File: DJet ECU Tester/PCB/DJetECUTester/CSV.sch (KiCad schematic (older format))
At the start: 1 part, among them U6 SFH617A-1X007T

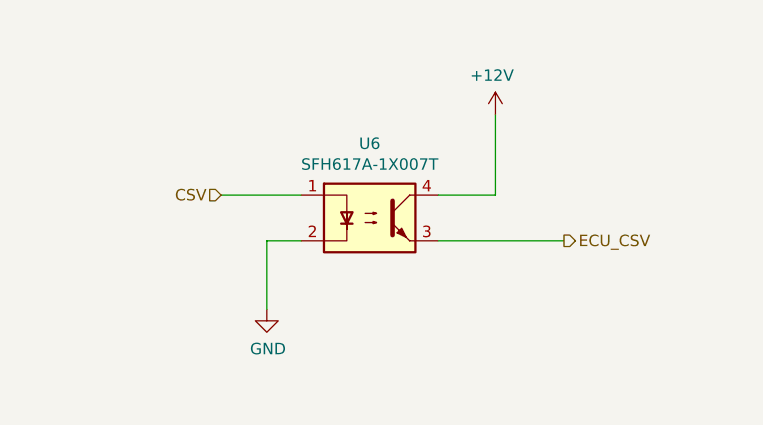
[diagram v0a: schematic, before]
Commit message: Working on PCB layout. Changed CSV circuit from optocoupler to transistors. Added decoupling caps for digital pots.
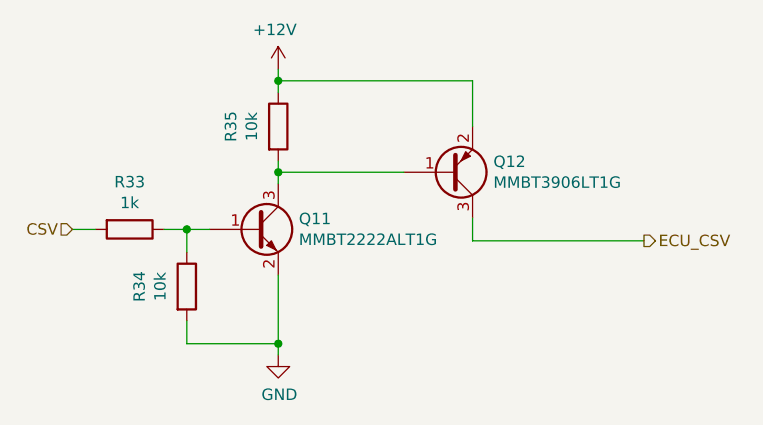
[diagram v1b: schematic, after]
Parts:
- removed U6: SFH617A-1X007T, Britishideas:SMD-4-OPTION7, symbol Isolator:SFH617A-1
- added Q11: MMBT2222ALT1G, Package_TO_SOT_SMD:SOT-23, symbol Transistor_BJT:MMBT3904
- added Q12: MMBT3906LT1G, Package_TO_SOT_SMD:SOT-23, symbol Device:Q_PNP_BEC
- added R33: 1k, Resistor_SMD:R_0805_2012Metric, symbol Device:R
- added R34, R35: 10k, Resistor_SMD:R_0805_2012Metric, symbol Device:R
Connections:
- net +12V: now also Q12.2 (E), R35.1
- net CSV: now also R33.2
- net ECU_CSV: now also Q12.3 (C)
- net GND: now also Q11.2 (E), R34.2
- new net: Q11.1 (B), R33.1, R34.1
- new net: Q11.3 (C), Q12.1 (B), R35.2
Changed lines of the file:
@@
 Sheet 7 7
 Title "D-Jetronic ECU Tester"
-Date "2021-03-08"
+Date "2021-03-09"
 Rev "1.0"
 Comp "(C) Britishideas 2021"
@@
 Comment4 ""
 $EndDescr
+Text HLabel 6950 4150 2    50   Output ~ 0
+ECU_CSV
+Text HLabel 4450 4100 0    50   Input ~ 0
+CSV
 $Comp
-L Isolator:SFH617A-1 U6
-U 1 1 6046F1A5
-P 5750 4050
-F 0 "U6" H 5750 4375 50  0000 C CNN
-F 1 "SFH617A-1X007T" H 5750 4284 50  0000 C CNN
-F 2 "Britishideas:SMD-4-OPTION7" H 5550 3850 50  0001 L CIN
-F 3 "http://www.vishay.com/docs/83740/sfh617a.pdf" H 5750 4050 50  0001 L CNN
-F 4 "SFH617A-1X007T" H 5750 4050 50  0001 C CNN "manf#"
-	1    5750 4050
+L Device:R R?
+U 1 1 60493C1A
+P 4700 4100
+AR Path="/604BF505/60493C1A" Ref="R?"  Part="1"
+AR Path="/60469920/60493C1A" Ref="R33"  Part="1"
+F 0 "R33" V 4493 4100 50  0000 C CNN
+F 1 "1k" V 4584 4100 50  0000 C CNN
+F 2 "Resistor_SMD:R_0805_2012Metric" V 4630 4100 50  0001 C CNN
+F 3 "~" H 4700 4100 50  0001 C CNN
+	1    4700 4100
+	0    1    1    0
+$EndComp
+$Comp
+L power:GND #PWR?
+U 1 1 60493C20
+P 5350 4650
+AR Path="/60493C20" Ref="#PWR?"  Part="1"
+AR Path="/604BF505/60493C20" Ref="#PWR?"  Part="1"
+AR Path="/60469920/60493C20" Ref="#PWR055"  Part="1"
+F 0 "#PWR055" H 5350 4400 50  0001 C CNN
+F 1 "GND" H 5355 4477 50  0000 C CNN
+F 2 "" H 5350 4650 50  0001 C CNN
+F 3 "" H 5350 4650 50  0001 C CNN
+	1    5350 4650
+	1    0    0    -1
+$EndComp
+Wire Wire Line
+	4450 4100 4550 4100
+$Comp
+L Transistor_BJT:MMBT3904 Q?
+U 1 1 60493C28
+P 5250 4100
+AR Path="/604BF505/60493C28" Ref="Q?"  Part="1"
+AR Path="/60469920/60493C28" Ref="Q11"  Part="1"
+F 0 "Q11" H 5440 4146 50  0000 L CNN
+F 1 "MMBT2222ALT1G" H 5440 4055 50  0000 L CNN
+F 2 "Package_TO_SOT_SMD:SOT-23" H 5450 4025 50  0001 L CIN
+F 3 "https://www.fairchildsemi.com/datasheets/2N/2N3904.pdf" H 5250 4100 50  0001 L CNN
+F 4 "MMBT2222ALT1G" H 5250 4100 50  0001 C CNN "manf#"
+	1    5250 4100
 	1    0    0    -1
 $EndComp
 $Comp
-L power:GND #PWR?
-U 1 1 6046FD16
-P 5300 4450
-AR Path="/6046FD16" Ref="#PWR?"  Part="1"
-AR Path="/604BF505/6046FD16" Ref="#PWR?"  Part="1"
-AR Path="/60469920/6046FD16" Ref="#PWR054"  Part="1"
-F 0 "#PWR054" H 5300 4200 50  0001 C CNN
-F 1 "GND" H 5305 4277 50  0000 C CNN
-F 2 "" H 5300 4450 50  0001 C CNN
-F 3 "" H 5300 4450 50  0001 C CNN
-	1    5300 4450
+L Device:R R?
+U 1 1 60493C2E
+P 4950 4350
+AR Path="/604BF505/60493C2E" Ref="R?"  Part="1"
+AR Path="/60469920/60493C2E" Ref="R34"  Part="1"
+F 0 "R34" V 4743 4350 50  0000 C CNN
+F 1 "10k" V 4834 4350 50  0000 C CNN
+F 2 "Resistor_SMD:R_0805_2012Metric" V 4880 4350 50  0001 C CNN
+F 3 "~" H 4950 4350 50  0001 C CNN
+	1    4950 4350
 	1    0    0    -1
 $EndComp
 Wire Wire Line
-	5450 4150 5300 4150
+	5350 3800 5350 3850
 Wire Wire Line
-	5300 4150 5300 4450
+	5350 4300 5350 4600
 Wire Wire Line
-	5450 3950 5100 3950
-Text HLabel 6600 4150 2    50   Output ~ 0
-ECU_CSV
-Text HLabel 5100 3950 0    50   Input ~ 0
-CSV
+	4850 4100 4950 4100
 Wire Wire Line
-	6600 4150 6050 4150
+	4950 4100 4950 4200
+Connection ~ 4950 4100
+Wire Wire Line
+	4950 4100 5050 4100
+Wire Wire Line
+	4950 4500 4950 4600
+Wire Wire Line
+	4950 4600 5350 4600
+Connection ~ 5350 4600
+Wire Wire Line
+	5350 4600 5350 4650
+$Comp
+L Device:Q_PNP_BEC Q12
+U 1 1 6049479C
+P 6100 3850
+F 0 "Q12" H 6291 3804 50  0000 L CNN
+F 1 "MMBT3906LT1G" H 6291 3895 50  0000 L CNN
+F 2 "Package_TO_SOT_SMD:SOT-23" H 6300 3950 50  0001 C CNN
+F 3 "~" H 6100 3850 50  0001 C CNN
+F 4 "MMBT3906LT1G" H 6100 3850 50  0001 C CNN "manf#"
+	1    6100 3850
+	1    0    0    1
+$EndComp
+$Comp
+L Device:R R?
+U 1 1 60494E3C
+P 5350 3650
+AR Path="/604BF505/60494E3C" Ref="R?"  Part="1"
+AR Path="/60469920/60494E3C" Ref="R35"  Part="1"
+F 0 "R35" V 5143 3650 50  0000 C CNN
+F 1 "10k" V 5234 3650 50  0000 C CNN
+F 2 "Resistor_SMD:R_0805_2012Metric" V 5280 3650 50  0001 C CNN
+F 3 "~" H 5350 3650 50  0001 C CNN
+	1    5350 3650
+	1    0    0    -1
+$EndComp
 $Comp
 L power:+12V #PWR?
-U 1 1 60470927
-P 6300 3600
-AR Path="/60470927" Ref="#PWR?"  Part="1"
-AR Path="/60479334/60470927" Ref="#PWR?"  Part="1"
-AR Path="/60469920/60470927" Ref="#PWR055"  Part="1"
-F 0 "#PWR055" H 6300 3450 50  0001 C CNN
-F 1 "+12V" H 6315 3773 50  0000 C CNN
-F 2 "" H 6300 3600 50  0001 C CNN
-F 3 "" H 6300 3600 50  0001 C CNN
-	1    6300 3600
+U 1 1 60495295
+P 5350 3400
+AR Path="/60495295" Ref="#PWR?"  Part="1"
+AR Path="/60479334/60495295" Ref="#PWR?"  Part="1"
+AR Path="/60469920/60495295" Ref="#PWR054"  Part="1"
+F 0 "#PWR054" H 5350 3250 50  0001 C CNN
+F 1 "+12V" H 5365 3573 50  0000 C CNN
+F 2 "" H 5350 3400 50  0001 C CNN
+F 3 "" H 5350 3400 50  0001 C CNN
+	1    5350 3400
 	-1   0    0    -1
 $EndComp
 Wire Wire Line
-	6300 3600 6300 3950
+	5350 3400 5350 3450
 Wire Wire Line
-	6300 3950 6050 3950
+	5900 3850 5350 3850
+Connection ~ 5350 3850
+Wire Wire Line
+	5350 3850 5350 3900
+Wire Wire Line
+	6200 3650 6200 3450
+Wire Wire Line
+	6200 3450 5350 3450
+Connection ~ 5350 3450
+Wire Wire Line
+	5350 3450 5350 3500
+Wire Wire Line
+	6200 4050 6200 4150
+Wire Wire Line
+	6200 4150 6950 4150
 $EndSCHEMATC

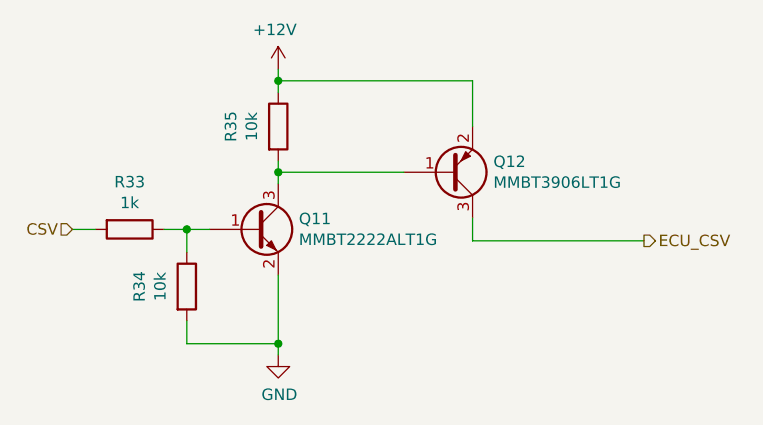
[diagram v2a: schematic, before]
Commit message: Added resistor to tester. Generated manufacturing files.
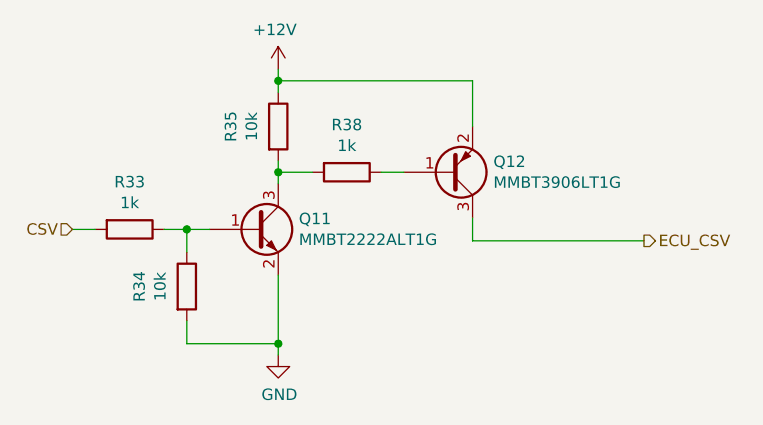
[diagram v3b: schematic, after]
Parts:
- added R38: 1k, Resistor_SMD:R_0805_2012Metric, symbol Device:R
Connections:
- net at Q11.3 (C), R35.2: now also R38.2; no longer Q12.1 (B)
- new net: Q12.1 (B), R38.1
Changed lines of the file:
@@
 Sheet 7 7
 Title "D-Jetronic ECU Tester"
-Date "2021-03-12"
+Date "2021-03-15"
 Rev "1.0"
 Comp "(C) Britishideas 2021"
@@
 $EndComp
 Wire Wire Line
-	5350 3800 5350 3850
-Wire Wire Line
 	5350 4300 5350 4600
 Wire Wire Line
@@
 	5350 3400 5350 3450
 Wire Wire Line
-	5900 3850 5350 3850
-Connection ~ 5350 3850
-Wire Wire Line
-	5350 3850 5350 3900
-Wire Wire Line
 	6200 3650 6200 3450
 Wire Wire Line
@@
 Wire Wire Line
 	6200 4150 6950 4150
+$Comp
+L Device:R R?
+U 1 1 6050F32C
+P 5650 3850
+AR Path="/604BF505/6050F32C" Ref="R?"  Part="1"
+AR Path="/60469920/6050F32C" Ref="R38"  Part="1"
+F 0 "R38" V 5443 3850 50  0000 C CNN
+F 1 "1k" V 5534 3850 50  0000 C CNN
+F 2 "Resistor_SMD:R_0805_2012Metric" V 5580 3850 50  0001 C CNN
+F 3 "~" H 5650 3850 50  0001 C CNN
+	1    5650 3850
+	0    1    1    0
+$EndComp
+Wire Wire Line
+	5350 3800 5350 3850
+Wire Wire Line
+	5800 3850 5900 3850
+Wire Wire Line
+	5500 3850 5350 3850
+Connection ~ 5350 3850
+Wire Wire Line
+	5350 3850 5350 3900
 $EndSCHEMATC
